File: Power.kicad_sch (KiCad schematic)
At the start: 35 parts, among them J3 XT60, Q2 DMG2301L, U7 TPS63060, U8 SPX3819M5-L-3-3

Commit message: feat: Comms complete
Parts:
- added D2: B5819W, Diode_SMD:D_SOD-123, symbol Device:D_Schottky_Small
- added D8: Green, LED_SMD:LED_0603_1608Metric, symbol Device:LED
- added R17: 4.7k, PCM_SparkFun-Resistor:R_0603_1608Metric, symbol PCM_SparkFun-Resistor:4.7k_0603
- added TP7: 1.0mm, PCM_SparkFun-Connector:TestPoint-1.0mm, symbol PCM_SparkFun-Connector:TestPoint_1.0mm
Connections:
- net GND: now also D8.1 (K)
- net VBAT_FUSED: now also D2.1 (K); no longer F2.1
- new net: D8.2 (A), R17.2
- new net VBAT_POLY_STATUS: D2.2 (A), F2.1, R17.1, TP7.1
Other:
- moved on the sheet: D3, D7, F2, R15, R9, TP3

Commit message: feat: Pyro done
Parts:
- J3: value XT60 -> BATT_XT60
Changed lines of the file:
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@@
 			)
 		)
-		(property "Value" "XT60"
+		(property "Value" "BATT_XT60"
 			(at 64.77 48.26 0)
 			(show_name no)

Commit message: feat: VBAT Sense
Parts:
- added R31: 33k, PCM_SparkFun-Resistor:R_0603_1608Metric, symbol PCM_SparkFun-Resistor:4.7k_0603
- added R32: 10k, PCM_SparkFun-Resistor:R_0603_1608Metric, symbol PCM_SparkFun-Resistor:4.7k_0603
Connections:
- net GND: now also R32.2
- net VBAT_PROT: now also R31.1
- new net VBAT_SENSE: R31.2, R32.1
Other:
- moved on the sheet: TP3

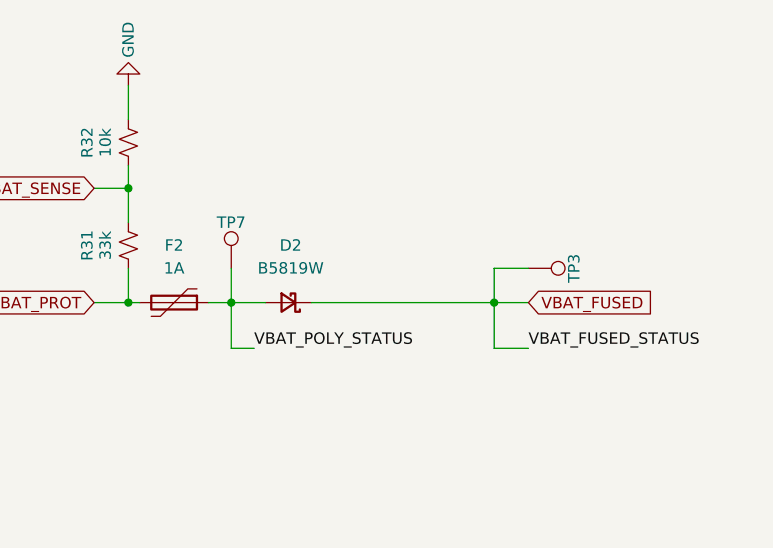
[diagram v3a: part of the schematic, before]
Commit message: feat: finish schematic (erc_pass)
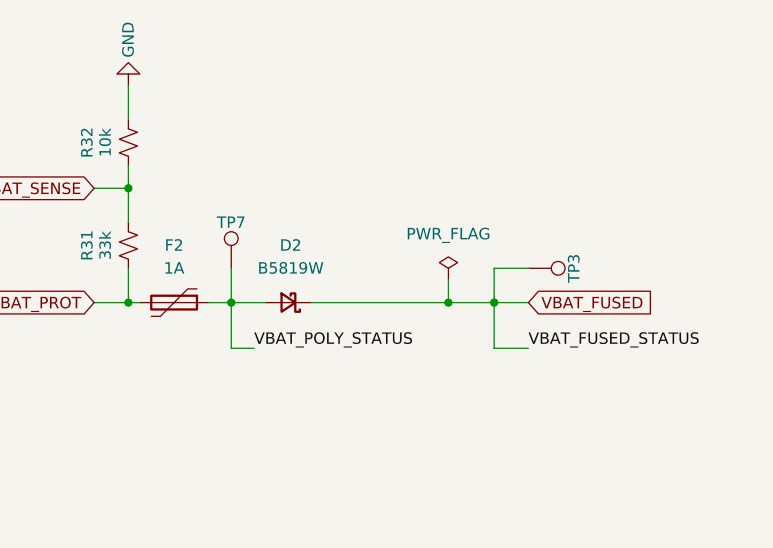
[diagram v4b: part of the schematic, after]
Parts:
- F2: footprint Fuse_1206_3216Metric -> Fuse:Fuse_1206_3216Metric
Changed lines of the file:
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@@
 	)
 	(junction
+		(at 237.49 52.07)
+		(diameter 0)
+		(color 0 0 0 0)
+	)
+	(junction
 		(at 213.36 52.07)
 		(diameter 0)
@@
 	(wire
 		(pts
+			(xy 237.49 49.53) (xy 237.49 52.07)
+		)
+		(stroke
+			(width 0)
+			(type default)
+		)
+	)
+	(wire
+		(pts
 			(xy 104.14 119.38) (xy 104.14 114.3)
 		)
@@
 	(wire
 		(pts
+			(xy 237.49 52.07) (xy 242.57 52.07)
+		)
+		(stroke
+			(width 0)
+			(type default)
+		)
+	)
+	(wire
+		(pts
 			(xy 144.78 63.5) (xy 144.78 59.69)
 		)
@@
 	(wire
 		(pts
-			(xy 222.25 52.07) (xy 242.57 52.07)
+			(xy 222.25 52.07) (xy 237.49 52.07)
 		)
 		(stroke
@@
 	)
 	(symbol
+		(lib_id "power:PWR_FLAG")
+		(at 237.49 49.53 0)
+		(unit 1)
+		(body_style 1)
+		(exclude_from_sim no)
+		(in_bom yes)
+		(on_board yes)
+		(in_pos_files yes)
+		(dnp no)
+		(fields_autoplaced yes)
+		(property "Reference" "#FLG01"
+			(at 237.49 47.625 0)
+			(hide yes)
+			(show_name no)
+			(do_not_autoplace no)
+			(effects
+				(font
+					(size 1.27 1.27)
+				)
+			)
+		)
+		(property "Value" "PWR_FLAG"
+			(at 237.49 44.45 0)
+			(show_name no)
+			(do_not_autoplace no)
+			(effects
+				(font
+					(size 1.27 1.27)
+				)
+			)
+		)
+		(property "Footprint" ""
+			(at 237.49 49.53 0)
+			(hide yes)
+			(show_name no)
+			(do_not_autoplace no)
+			(effects
+				(font
+					(size 1.27 1.27)
+				)
+			)
+		)
+		(property "Datasheet" ""
+			(at 237.49 49.53 0)
+			(hide yes)
+			(show_name no)
+			(do_not_autoplace no)
+			(effects
+				(font
+					(size 1.27 1.27)
+				)
+			)
+		)
+		(property "Description" "Special symbol for telling ERC where power comes from"
+			(at 237.49 49.53 0)
+			(hide yes)
+			(show_name no)
+			(do_not_autoplace no)
+			(effects
+				(font
+					(size 1.27 1.27)
+				)
+			)
+		)
+		(pin "1"
+		)
+		(instances
+			(project "UNSW_Rocketry_Senior_Flight_Computer"
+				(path "/9e0253f5-fba5-4205-8256-7fc47a91dd1e/32dc7f8f-d1cd-4967-8830-7944681bf161"
+					(reference "#FLG01")
+					(unit 1)
+				)
+			)
+		)
+	)
+	(symbol
 		(lib_id "PCM_SparkFun-Capacitor:10uF_0805_25V_10%")
 		(at 67.31 111.76 180)
@@
 			)
 		)
-		(property "Footprint" "Fuse_1206_3216Metric"
+		(property "Footprint" "Fuse:Fuse_1206_3216Metric"
 			(at 201.93 53.34 0)
 			(hide yes)

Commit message: feat: finish schematic (Full)
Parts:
- renumbered C24 to C14, C26 to C16, C27 to C17, C17 to C18, C29 to C19, C18 to C20, C31 to C21, C33 to C23, D6 to D1, D7 to D3, D3 to D4, D8 to D5, D4 to D6, D5 to D7, F2 to F1, J3 to J1, L2 to L1, Q2 to Q1, R17 to R10, R16 to R11, R7 to R12, R4 to R2, R5 to R3, R12 to R4, R13 to R5, R32 to R6, R31 to R7, R9 to R8, R15 to R9, TP10 to TP1, TP4 to TP2, TP9 to TP3, TP6 to TP4, TP7 to TP6, TP3 to TP7, U7 to U2, U8 to U3
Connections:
- no-connect marks 0 -> 2
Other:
- moved on the sheet: J1
